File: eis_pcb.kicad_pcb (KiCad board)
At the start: 6 copper layers, 86 parts, among them J1 527451897, J12 104031-0811, J2 GSB1C41110SSHR, J4 541020164, P1 V.BATT, P2 GND.BATT, Q3 IRLML6344TRPBF, SW1 RST, SW2 BOOT, U1 ESP32-S3-WROOM-1-N8R8, U2 AD5941BCPZ, U3 TMUX1109RSVR, U4 LSM6DSVTR, U5 BQ24075RGT, U6 NCP186AMX330TAG

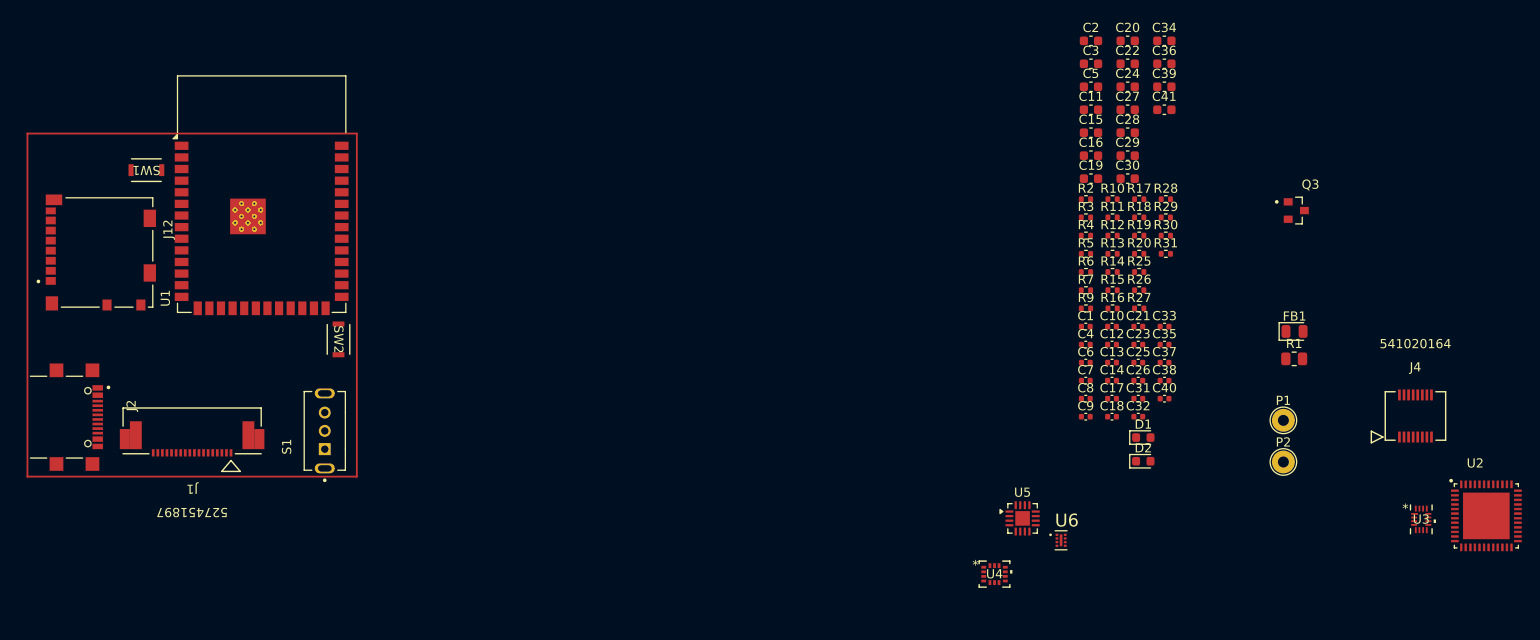
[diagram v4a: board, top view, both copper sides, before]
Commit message: finish rev B schematic
did some layout planning
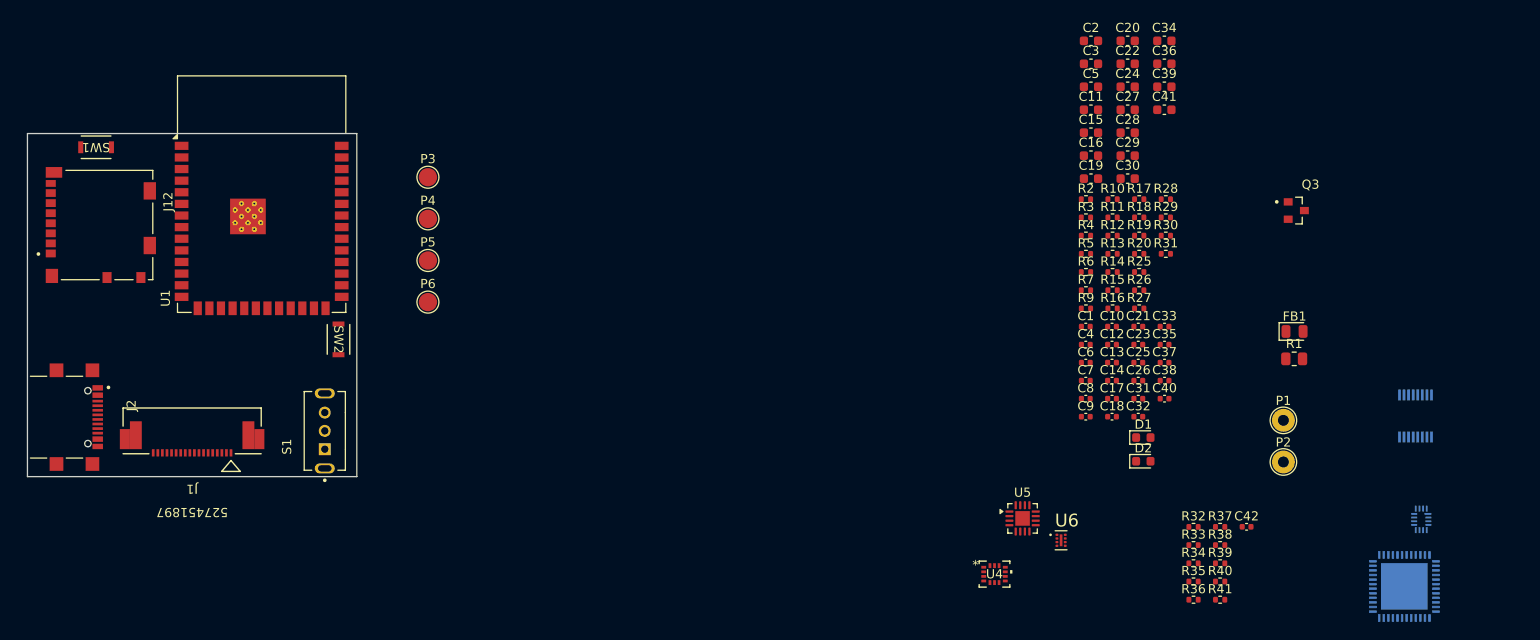
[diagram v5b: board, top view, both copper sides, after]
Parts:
- added C42: 100n, Capacitor_SMD:C_0402_1005Metric, F.Cu at (233.3, 123.0)
- added P3: DATA+, TestPoint:TestPoint_Pad_D2.0mm, F.Cu at (143.8, 84.8)
- added P4: DATA-, TestPoint:TestPoint_Pad_D2.0mm, F.Cu at (143.8, 89.3)
- added P5: RXD0, TestPoint:TestPoint_Pad_D2.0mm, F.Cu at (143.8, 93.9)
- added P6: TXD0, TestPoint:TestPoint_Pad_D2.0mm, F.Cu at (143.8, 98.4)
- added R32: 10k, Resistor_SMD:R_0402_1005Metric, F.Cu at (227.5, 123.0)
- added R33: 10k, Resistor_SMD:R_0402_1005Metric, F.Cu at (227.5, 125.0)
- added R34: 10k, Resistor_SMD:R_0402_1005Metric, F.Cu at (227.5, 127.0)
- added R35: 10k, Resistor_SMD:R_0402_1005Metric, F.Cu at (227.5, 129.0)
- added R36: 10k, Resistor_SMD:R_0402_1005Metric, F.Cu at (227.5, 131.0)
- added R37: 10k, Resistor_SMD:R_0402_1005Metric, F.Cu at (230.4, 123.0)
- added R38: 10k, Resistor_SMD:R_0402_1005Metric, F.Cu at (230.4, 125.0)
- added R39: 10k, Resistor_SMD:R_0402_1005Metric, F.Cu at (230.4, 127.0)
- added R40: 10k, Resistor_SMD:R_0402_1005Metric, F.Cu at (230.4, 129.0)
- added R41: 10k, Resistor_SMD:R_0402_1005Metric, F.Cu at (230.4, 131.0)
- J4, U2, U3: moved to B.Cu
- R28, R29, R30, R31: value 4.7k -> 10k
- moved U2 11.8 mm to (250.5, 129.5), turned to 180 degrees
- moved SW1 6.04 mm to (107.5, 81.5)
- moved J12 3.00 mm to (108.0, 90.0)
- turned J4 to 180 degrees
- turned U3 to 180 degrees
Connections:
- C29 pad 1: Net-(C29-Pad1) -> +VSYS
- C32 pad 2: Net-(C29-Pad1) -> +VSYS
- C34 pad 1: GND -> +5V
- C34 pad 2: +5V -> GND
- C4 pad 1: /DVDD.1V8 -> /AVDD.REG
- C6 pad 1: /REF.2V5 -> /DVDD.1V8
- C7 pad 1: /BIAS.CAP -> /REF.2V5
- C8 pad 1: /AVDD.REG -> /BIAS.CAP
- J12 pad 1: unconnected-(J12-DAT2-Pad1) -> /DAT2
- J12 pad 10: GND -> /CD
- J12 pad 2: /CS.SD -> /DAT3
- J12 pad 3: /MOSI -> /CMD
- J12 pad 5: /SCLK -> /CLK
- J12 pad 7: /MISO -> /DAT0
- J12 pad 8: unconnected-(J12-DAT1-Pad8) -> /DAT1
- J12 pad 9: /SW1 -> GND
- R16 pad 1: Net-(Q3-Pad3) -> /K
- R16 pad 2: /K -> Net-(Q3-Pad3)
- R26 pad 1: /CS.AFE -> /SDA.TOUCH
- R27 pad 1: Net-(U1-IO39) -> /SCL.TOUCH
- R28 pad 1: /CS.SD -> /CMD
- R29 pad 1: Net-(U1-IO41) -> /DAT0
- R30 pad 1: Net-(U1-IO42) -> /DAT1
- R31 pad 1: /CS.IMU -> /DAT2
- R7 pad 1: Net-(U2-DVDD) -> +3V3
- R7 pad 2: +3V3 -> Net-(U2-DVDD)
- U1 pad 10: unconnected-(U1-IO17-Pad10) -> /MISO
- U1 pad 11: unconnected-(U1-IO18-Pad11) -> /INT.TOUCH
- U1 pad 12: unconnected-(U1-IO8-Pad12) -> /RST.TOUCH
- U1 pad 22: unconnected-(U1-IO14-Pad22) -> /PWM.SCREEN
- U1 pad 23: /SCREEN.RST -> /INT.IMU
- U1 pad 24: /CTP_RST -> /CS.IMU
- U1 pad 25: /CTP_INT -> /CD
- U1 pad 26: /CS.IMU -> unconnected-(U1-IO45-Pad26)
- U1 pad 31: unconnected-(U1-IO38-Pad31) -> /CS.AFE
- U1 pad 32: Net-(U1-IO39) -> /RST.AFE
- U1 pad 33: /CS.SD -> /EN.MUX
- U1 pad 34: Net-(U1-IO41) -> /A0.MUX
- U1 pad 35: Net-(U1-IO42) -> /A1.MUX
- U1 pad 36: unconnected-(U1-RXD0-Pad36) -> /RXD0
- U1 pad 37: unconnected-(U1-TXD0-Pad37) -> /TXD0
- U1 pad 38: unconnected-(U1-IO2-Pad38) -> /SDA.TOUCH
- U1 pad 39: unconnected-(U1-IO1-Pad39) -> /IO1
- U1 pad 4: unconnected-(U1-IO4-Pad4) -> /V.BATT.SENSE
- U1 pad 5: unconnected-(U1-IO5-Pad5) -> /DAT0
- U1 pad 6: unconnected-(U1-IO6-Pad6) -> /CLK
- U1 pad 7: unconnected-(U1-IO7-Pad7) -> /CMD
- U1 pad 8: unconnected-(U1-IO15-Pad8) -> /SCLK
- U1 pad 9: unconnected-(U1-IO16-Pad9) -> /MOSI
- U5 pad 10: Net-(C29-Pad1) -> +VSYS
- U5 pad 11: Net-(C29-Pad1) -> +VSYS
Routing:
- added copper zone on In1.Cu, net GND
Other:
- board outline added: 36 x 37.5 mm

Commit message: remove redundant caps
removed some decoupling caps in power circuit because the components were so close together
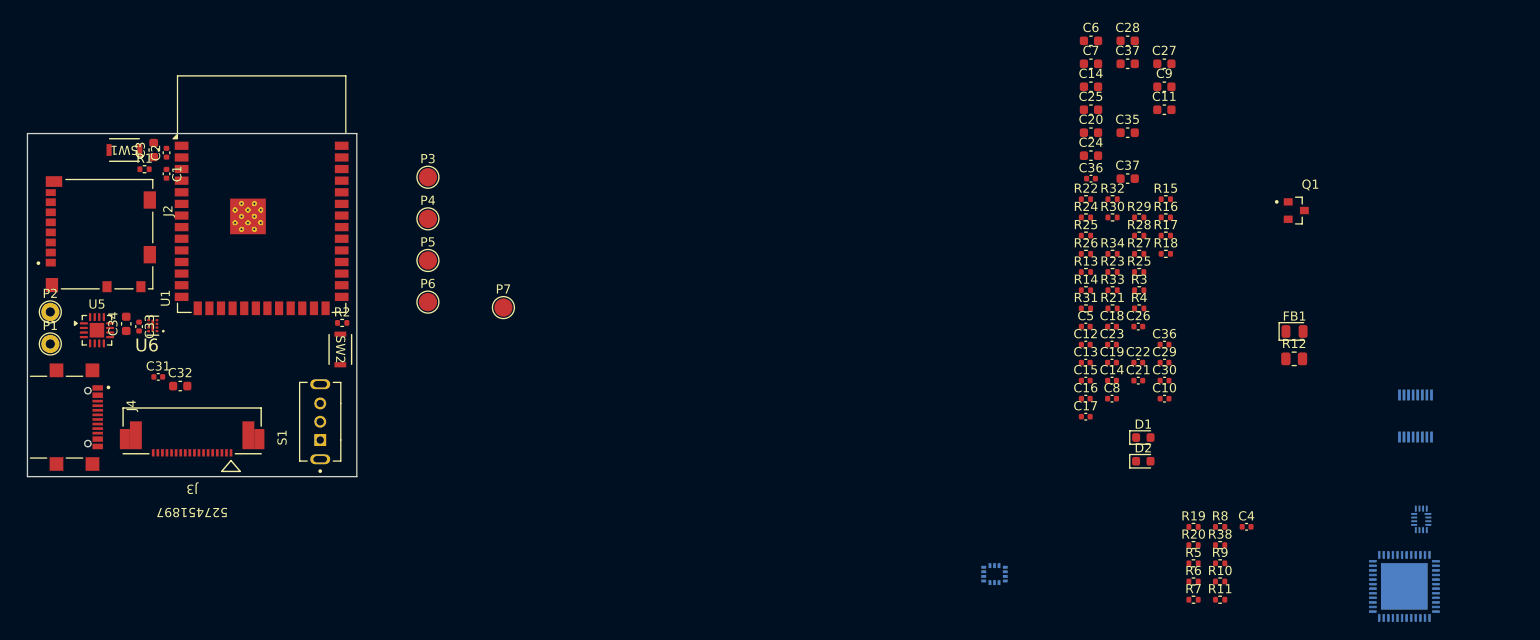
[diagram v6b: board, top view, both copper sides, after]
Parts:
- removed the C33 at (224.3, 101.1)
- removed the C34 at (224.3, 69.9)
- added P7: IO1, TestPoint:TestPoint_Pad_D2.0mm, F.Cu at (152.0, 99.0)
- C36: renamed from C19; footprint Capacitor_SMD:C_0603_1608Metric -> Capacitor_SMD:C_0402_1005Metric
- P1: value V.BATT -> +BATT; footprint TestPoint:TestPoint_THTPad_D2.5mm_Drill1.2mm -> TestPoint:TestPoint_THTPad_D2.0mm_Drill1.0mm
- P2: value GND.BATT -> GND; footprint TestPoint:TestPoint_THTPad_D2.5mm_Drill1.2mm -> TestPoint:TestPoint_THTPad_D2.0mm_Drill1.0mm
- U4: moved to B.Cu
- moved P2 135.8 mm to (102.5, 99.5)
- moved P1 135.0 mm to (102.5, 103.0)
- moved C34 111.0 mm to (110.8, 100.8), turned to 90 degrees
- moved C33 109.7 mm to (112.2, 101.1), turned to -90 degrees
- moved C2 108.3 mm to (115.2, 82.1), turned to 90 degrees
- moved C32 107.9 mm to (116.7, 107.6)
- moved C31 107.1 mm to (114.3, 106.6)
- moved C1 106.7 mm to (115.2, 84.4), turned to -90 degrees
- moved C3 106.7 mm to (113.8, 81.8), turned to 90 degrees
- moved R1 106.1 mm to (112.8, 83.9)
- moved U5 103.2 mm to (107.6, 101.5)
- moved U6 102.0 mm to (113.7, 101.0), turned to 180 degrees
- moved R2 88.2 mm to (134.4, 100.7)
- moved SW1 3.11 mm to (110.6, 81.8)
- moved S1 1.12 mm to (132.0, 111.5)
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- renumbered C18 to C1, C40 to C10, C41 to C11, C4 to C12, C6 to C13, C5 to C14, C7 to C15, C8 to C16, C9 to C17, C10 to C18, C13 to C19, C23 to C2, C15 to C20, C26 to C21, C25 to C22, C12 to C23, C16 to C24, C11 to C25, C21 to C26, C36 to C27, C20 to C28, C37 to C29, C24 to C3, C38 to C30, C27 to C32, C32 to C33, C29 to C34, C28 to C35, C35 to C36, C30 to C37, C22 to C37, C42 to C4, C1 to C5, C2 to C6, C3 to C7, C17 to C8, C39 to C9, J4 to J1, J12 to J2, J1 to J3, J2 to J4, Q3 to Q1, R12 to R1, R40 to R10, R41 to R11, R1 to R12, R6 to R13, R7 to R14, R28 to R15, R29 to R16, R30 to R17, R31 to R18, R32 to R19, R17 to R2, R33 to R20, R16 to R21, R2 to R22, R14 to R23, R3 to R24, R4 to R25, R5 to R26, R20 to R27, R19 to R28, R18 to R29, R26 to R3, R11 to R30, R9 to R31, R10 to R32, R15 to R33, R13 to R34, R27 to R4, R34 to R5, R35 to R6, R36 to R7, R37 to R8, R39 to R9

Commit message: begin power layout
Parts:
- moved R29 116.6 mm to (105.3, 98.8), turned to 180 degrees
- moved R30 114.3 mm to (104.9, 100.4), turned to 90 degrees
- moved R27 114.3 mm to (107.4, 98.8)
- moved U5 0.13 mm to (107.7, 101.6)
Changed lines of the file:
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@@
 		(capping no)
 		(filling no)
-		(zone_defaults)
 		(pcbplotparams
 			(layerselection 0x00000000_00000000_55555555_5755f5ff)
@@
 	(footprint "Package_DFN_QFN:VQFN-16-1EP_3x3mm_P0.5mm_EP1.6x1.6mm"
 		(layer "F.Cu")
-		(at 107.6 101.5)
+		(at 107.6875 101.6)
 		(descr "VQFN, 16 Pin (http://www.ti.com/lit/ds/symlink/cdclvp1102.pdf#page=28)")
 		(tags "VQFN NoLead")
@@
 	(footprint "Resistor_SMD:R_0402_1005Metric"
 		(layer "F.Cu")
-		(at 218.6084 89.1684)
+		(at 104.9 100.4 90)
 		(descr "Resistor SMD 0402 (1005 Metric), square (rectangular) end terminal, IPC-7351 nominal, (Body size source: IPC-SM-782 page 72, https://www.pcb-3d.com/wordpress/wp-content/uploads/ipc-sm-782a_amendment_1_and_2.pdf)")
 		(tags "resistor")
 		(property "Reference" "R30"
-			(at 0 -1.17 0)
+			(at 0 -1.17 90)
 			(layer "F.SilkS")
 			(effects
@@
 		)
 		(property "Value" "10k"
-			(at 0 1.17 0)
+			(at 0 1.17 90)
 			(layer "F.Fab")
 			(effects
@@
 		)
 		(property "Datasheet" ""
-			(at 0 0 0)
+			(at 0 0 90)
 			(layer "F.Fab")
 			(hide yes)
@@
 		)
 		(property "Description" "Resistor, small symbol"
-			(at 0 0 0)
+			(at 0 0 90)
 			(layer "F.Fab")
 			(hide yes)
@@
 		)
 		(property "KiLib_Generator" "SMD_2terminal_chip_molded"
-			(at 0 0 0)
+			(at 0 0 90)
 			(layer "F.SilkS")
 			(hide yes)
@@
 		)
 		(fp_text user "${REFERENCE}"
-			(at 0 0 0)
+			(at 0 0 90)
 			(layer "F.Fab")
 			(effects
@@
 		)
 		(pad "1" smd roundrect
-			(at -0.51 0)
+			(at -0.51 0 90)
 			(size 0.54 0.64)
 			(layers "F.Cu" "F.Mask" "F.Paste")
@@
 		)
 		(pad "2" smd roundrect
-			(at 0.51 0)
+			(at 0.51 0 90)
 			(size 0.54 0.64)
 			(layers "F.Cu" "F.Mask" "F.Paste")
@@
 	(footprint "Resistor_SMD:R_0402_1005Metric"
 		(layer "F.Cu")
-		(at 221.5184 89.1684)
+		(at 105.3 98.8 180)
 		(descr "Resistor SMD 0402 (1005 Metric), square (rectangular) end terminal, IPC-7351 nominal, (Body size source: IPC-SM-782 page 72, https://www.pcb-3d.com/wordpress/wp-content/uploads/ipc-sm-782a_amendment_1_and_2.pdf)")
 		(tags "resistor")
@@
 		(duplicate_pad_numbers_are_jumpers no)
 		(fp_line
-			(start -0.153641 -0.38)
-			(end 0.153641 -0.38)
+			(start -0.153641 0.38)
+			(end 0.153641 0.38)
 			(stroke
 				(width 0.12)
@@
 		)
 		(fp_line
-			(start -0.153641 0.38)
-			(end 0.153641 0.38)
+			(start -0.153641 -0.38)
+			(end 0.153641 -0.38)
 			(stroke
 				(width 0.12)
@@
 		)
 		(pad "1" smd roundrect
-			(at -0.51 0)
+			(at -0.51 0 180)
 			(size 0.54 0.64)
 			(layers "F.Cu" "F.Mask" "F.Paste")
@@
 		)
 		(pad "2" smd roundrect
-			(at 0.51 0)
+			(at 0.51 0 180)
 			(size 0.54 0.64)
 			(layers "F.Cu" "F.Mask" "F.Paste")
@@
 	(footprint "Resistor_SMD:R_0402_1005Metric"
 		(layer "F.Cu")
-		(at 221.5184 93.1484)
+		(at 107.4 98.8)
 		(descr "Resistor SMD 0402 (1005 Metric), square (rectangular) end terminal, IPC-7351 nominal, (Body size source: IPC-SM-782 page 72, https://www.pcb-3d.com/wordpress/wp-content/uploads/ipc-sm-782a_amendment_1_and_2.pdf)")
 		(tags "resistor")

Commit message: finish layout
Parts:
- removed the C14 at (218.5, 107.0)
- removed the C29 at (224.3, 105.0)
- removed the C36 at (224.3, 103.1)
- removed C37: 1u, Capacitor_SMD:C_0603_1608Metric
- removed the R25 at (221.5, 95.1)
- removed R38: 10k, Resistor_SMD:R_0402_1005Metric
- C10, C11, C12, C13, C14, C15, C16, C17, C18, C19, C20, C21, C22, C23, C24, C25, C26, C27, C28, C5, C6, C7, C8, C9, FB1, R10, R11, R12, R13, R14, R16, R17, R18, R19, R20, R6, R7, R8: moved to B.Cu
- P3, P4, P5, P6, P7: footprint TestPoint:TestPoint_Pad_D2.0mm -> TestPoint:TestPoint_Pad_D1.5mm; moved to B.Cu
- moved J1 134.6 mm to (118.0, 95.5), turned to 90 degrees
- moved C4 128.7 mm to (110.6, 83.9)
- moved R20 128.4 mm to (105.0, 86.5)
- moved U3 127.7 mm to (127.5, 95.5), turned to -90 degrees
- moved U2 127.6 mm to (125.0, 106.5)
- moved R19 127.5 mm to (105.0, 87.5)
- moved R8 121.5 mm to (111.9, 95.8), turned to 180 degrees
- moved R12 119.6 mm to (118.9, 105.2)
- moved R16 119.5 mm to (105.0, 94.1)
- moved R17 119.4 mm to (105.0, 93.0)
- moved R18 119.4 mm to (105.0, 91.9)
- moved C34 115.7 mm to (106.8, 102.7), turned to -90 degrees
- moved C23 114.2 mm to (105.0, 90.8)
- moved R9 112.8 mm to (120.5, 101.3), turned to 90 degrees
- moved Q1 111.4 mm to (128.7, 106.3)
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- renumbered C30 to C29, C31 to C30, C32 to C31, C33 to C32, C34 to C33, C35 to C34, C36 to C35, C37 to C36
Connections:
- J1 pad 12: /WE3 -> /WE2
- J1 pad 13: /WE4 -> /WE1
- J1 pad 15: /CE3 -> /CE1
- J1 pad 16: /CE4 -> /CE2
- J1 pad 4: /WE1 -> /WE4
- J1 pad 5: /WE2 -> /WE3
- J1 pad 7: /CE1 -> /CE3
- J1 pad 8: /CE2 -> /CE4
- R15 pad 1: /CMD -> /CD
- R16 pad 1: /DAT0 -> /DAT2
- R17 pad 1: /DAT1 -> /DAT3
- R18 pad 1: /DAT2 -> /CMD
- R19 pad 1: /DAT3 -> /DAT0
- R20 pad 1: /CD -> /DAT1
- S1 pad SH1: (no net) -> GND
- S1 pad SH2: (no net) -> GND
- U1 pad 23: /INT.IMU -> /SDA.TOUCH
- U1 pad 33: /EN.MUX -> /A1.MUX
- U1 pad 35: /A1.MUX -> /EN.MUX
- U1 pad 38: /SDA.TOUCH -> /INT.IMU
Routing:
- net GND: track 0.00 -> 91.9 mm, vias 0 -> 10
- net +3V3: track 0.05 -> 76.8 mm, vias 0 -> 15
- net +VSYS: track 0.00 -> 57.4 mm, vias 0 -> 1
- net /MISO: track 0.00 -> 48.1 mm, vias 0 -> 2
- net /MOSI: track 0.00 -> 46.5 mm, vias 0 -> 2
- net /SCLK: track 0.00 -> 46.1 mm, vias 0 -> 2
- net /PWR.EN: track 0.00 -> 35.0 mm, vias 0 -> 1
- net /DATA-: track 0.00 -> 34.0 mm, vias 0 -> 1
- net /RST.AFE: track 0.00 -> 33.6 mm, vias 0 -> 2
- net /DATA+: track 0.00 -> 32.6 mm, vias 0 -> 1
- net +5V: track 0.00 -> 31.7 mm
- net /RE0: track 0.00 -> 28.9 mm
- net /CD: track 0.00 -> 28.4 mm, vias 0 -> 2
- net +BATT: track 0.00 -> 27.9 mm, vias 0 -> 1
- net /CS.AFE: track 0.00 -> 27.0 mm, vias 0 -> 2
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- added copper zone on In3.Cu, net +3V3
- added copper zone on In3.Cu, net /3V3A
- added copper zone on B.Cu, net GND
- added copper zone on F.Cu, net GND
- added copper zone on In2.Cu, net GND
- added copper zone on In4.Cu, net GND
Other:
- outline, holes or cut-outs redrawn
